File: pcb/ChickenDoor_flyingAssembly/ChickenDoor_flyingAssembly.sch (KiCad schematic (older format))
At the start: 3 parts

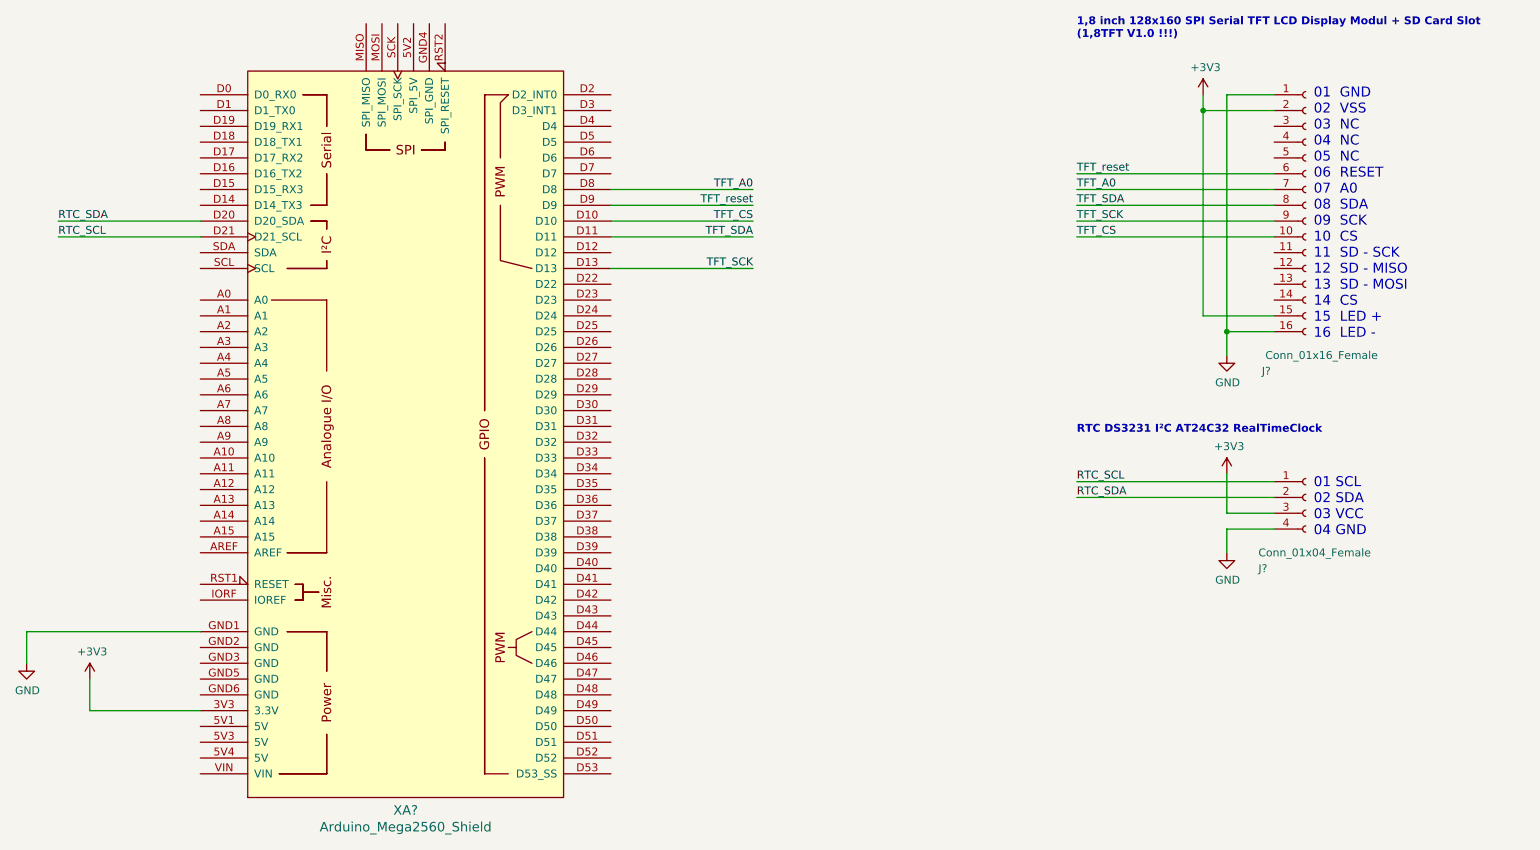
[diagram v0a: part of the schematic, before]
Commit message: some small changes in the schematic of the flying assembly.
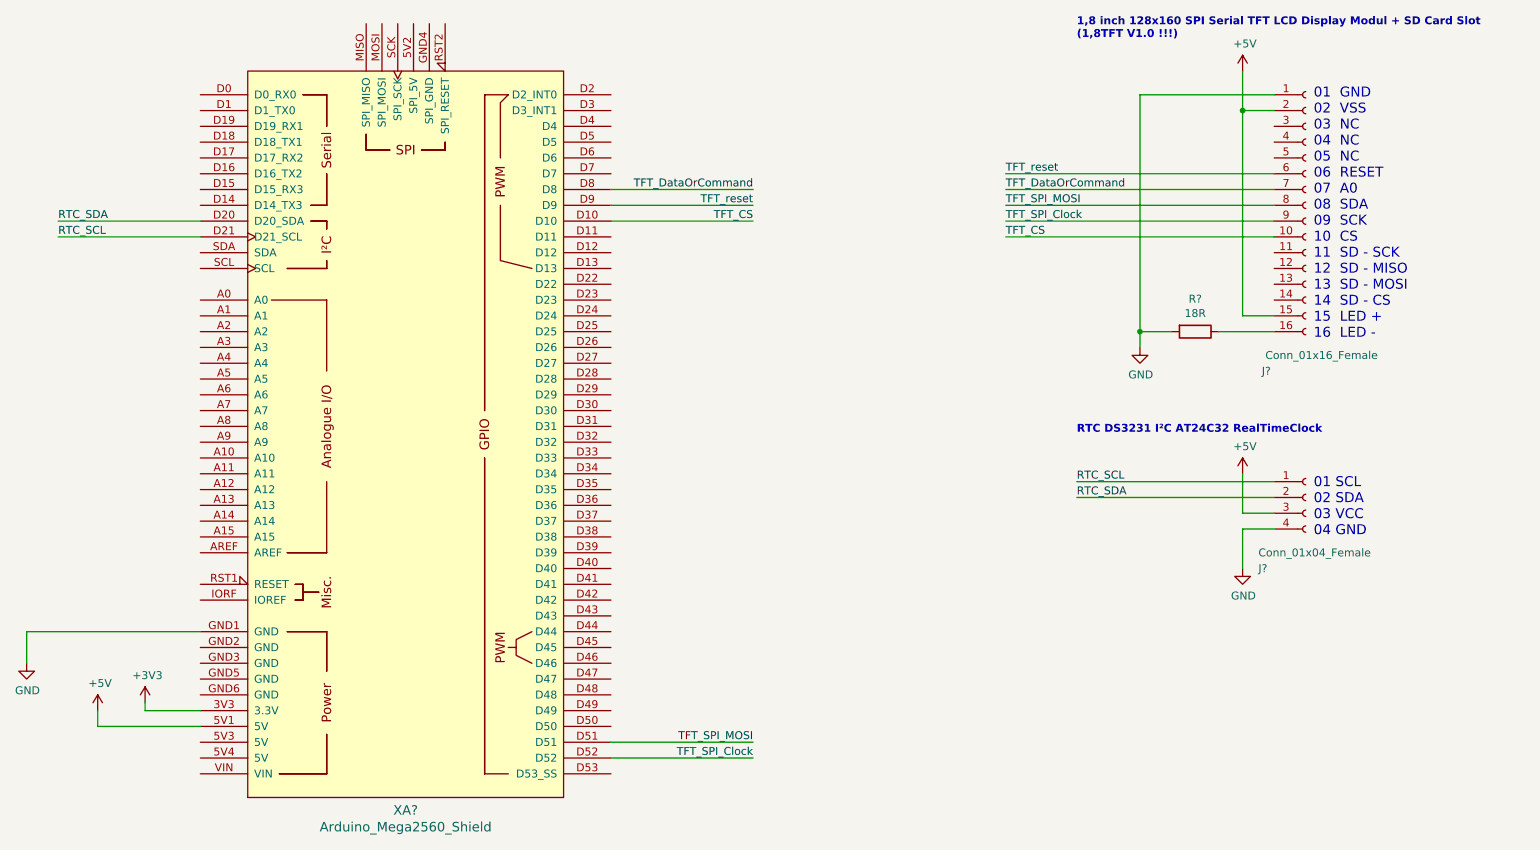
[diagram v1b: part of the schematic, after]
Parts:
- added R?: 18R, symbol Device:R
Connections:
- net +3V3: no longer J?.15 (Pin_15), J?.2 (Pin_2), J?.3 (Pin_3)
- net GND: now also R?.2; no longer J?.16 (Pin_16)
- net +5V: now reaches XA?.5V1 (5V)
- net +5V: now also J?.15 (Pin_15), J?.2 (Pin_2), J?.3 (Pin_3)
- net TFT_SPI_MOSI: now reaches XA?.D51
- net TFT_SPI_MOSI: now also J?.8 (Pin_8)
- net TFT_SPI_Clock: now reaches XA?.D52
- net TFT_SPI_Clock: now also J?.9 (Pin_9)
- net TFT_A0 renamed TFT_DataOrCommand
- net TFT_SCK: no longer names the net of XA?.D13
- net TFT_SCK: no longer J?.9 (Pin_9)
- net TFT_SDA: no longer names the net of XA?.D11
- net TFT_SDA: no longer J?.8 (Pin_8)
- new net: J?.16 (Pin_16), R?.1
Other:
- note added: "01 GND\n02 VSS\n03 NC\n04 NC\n05 NC\n06 RESET\n07 A0\n08 SDA\n09 SCK\n10 CS\n11 SD - SCK\n12 SD - MISO\n13 SD - MOSI\n14 SD - CS\n15 LED +\n16 LED -"
- note removed: "01 GND\n02 VSS\n03 NC\n04 NC\n05 NC\n06 RESET\n07 A0\n08 SDA\n09 SCK\n10 CS\n11 SD - SCK\n12 SD - MISO\n13 SD - MOSI\n14 CS\n15 LED +\n16 LED -"
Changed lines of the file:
@@
 L power:GND #PWR?
 U 1 1 5EDDCCDC
-P 8900 3250
-F 0 "#PWR?" H 8900 3000 50  0001 C CNN
-F 1 "GND" H 8905 3077 50  0000 C CNN
-F 2 "" H 8900 3250 50  0001 C CNN
-F 3 "" H 8900 3250 50  0001 C CNN
-	1    8900 3250
+P 8350 3200
+F 0 "#PWR?" H 8350 2950 50  0001 C CNN
+F 1 "GND" H 8355 3027 50  0000 C CNN
+F 2 "" H 8350 3200 50  0001 C CNN
+F 3 "" H 8350 3200 50  0001 C CNN
+	1    8350 3200
 	1    0    0    -1
 $EndComp
 Wire Wire Line
-	8900 3250 8900 3100
+	8350 3200 8350 3100
 Wire Wire Line
-	8900 3100 9200 3100
+	8350 3100 8550 3100
 Wire Wire Line
-	8900 3100 8900 1600
+	8350 3100 8350 1600
 Wire Wire Line
-	8900 1600 9200 1600
+	8350 1600 9200 1600
 $Comp
 L power:+3V3 #PWR?
 U 1 1 5EDDDAF5
-P 1700 5300
-F 0 "#PWR?" H 1700 5150 50  0001 C CNN
-F 1 "+3V3" H 1715 5473 50  0000 C CNN
-F 2 "" H 1700 5300 50  0001 C CNN
-F 3 "" H 1700 5300 50  0001 C CNN
-	1    1700 5300
+P 2050 5450
+F 0 "#PWR?" H 2050 5300 50  0001 C CNN
+F 1 "+3V3" H 2065 5623 50  0000 C CNN
+F 2 "" H 2050 5450 50  0001 C CNN
+F 3 "" H 2050 5450 50  0001 C CNN
+	1    2050 5450
 	1    0    0    -1
 $EndComp
 Wire Wire Line
-	2400 5500 1700 5500
+	2400 5500 2050 5500
 Wire Wire Line
-	1700 5500 1700 5300
-Connection ~ 8900 3100
-$Comp
-L power:+3V3 #PWR?
-U 1 1 5EDDF72B
-P 8750 1600
-F 0 "#PWR?" H 8750 1450 50  0001 C CNN
-F 1 "+3V3" H 8765 1773 50  0000 C CNN
-F 2 "" H 8750 1600 50  0001 C CNN
-F 3 "" H 8750 1600 50  0001 C CNN
-	1    8750 1600
-	1    0    0    -1
-$EndComp
+	2050 5500 2050 5450
+Connection ~ 8350 3100
+Text Notes 9450 3150 0    63   ~ 0
+01  GND\n02  VSS\n03  NC\n04  NC\n05  NC\n06  RESET\n07  A0\n08  SDA\n09  SCK\n10  CS\n11  SD - SCK\n12  SD - MISO\n13  SD - MOSI\n14  SD - CS\n15  LED +\n16  LED -
 Wire Wire Line
-	9200 1700 8750 1700
+	9200 3000 9000 3000
 Wire Wire Line
-	8750 1700 8750 1600
-Text Notes 9450 3150 0    63   ~ 0
-01  GND\n02  VSS\n03  NC\n04  NC\n05  NC\n06  RESET\n07  A0\n08  SDA\n09  SCK\n10  CS\n11  SD - SCK\n12  SD - MISO\n13  SD - MOSI\n14  CS\n15  LED +\n16  LED -
+	9200 2100 7500 2100
 Wire Wire Line
-	9200 3000 8750 3000
+	9200 2200 7500 2200
 Wire Wire Line
-	8750 3000 8750 1700
-Connection ~ 8750 1700
+	9200 2300 7500 2300
 Wire Wire Line
-	9200 2100 7950 2100
+	9200 2400 7500 2400
 Wire Wire Line
-	9200 2200 7950 2200
-Wire Wire Line
-	9200 2300 7950 2300
-Wire Wire Line
-	9200 2400 7950 2400
-Wire Wire Line
-	9200 2500 7950 2500
-Text Label 7950 2100 0    50   ~ 0
+	9200 2500 7500 2500
+Text Label 7500 2100 0    50   ~ 0
 TFT_reset
-Text Label 7950 2200 0    50   ~ 0
-TFT_A0
-Text Label 7950 2300 0    50   ~ 0
-TFT_SDA
-Text Label 7950 2400 0    50   ~ 0
-TFT_SCK
-Text Label 7950 2500 0    50   ~ 0
+Text Label 7500 2200 0    50   ~ 0
+TFT_DataOrCommand
+Text Label 7500 2300 0    50   ~ 0
+TFT_SPI_MOSI
+Text Label 7500 2400 0    50   ~ 0
+TFT_SPI_Clock
+Text Label 7500 2500 0    50   ~ 0
 TFT_CS
 Wire Wire Line
@@
 	5000 2400 5900 2400
 Wire Wire Line
-	5000 2500 5900 2500
+	5000 5700 5900 5700
 Wire Wire Line
-	5000 2700 5900 2700
+	5000 5800 5900 5800
 Text Label 5900 2200 2    50   ~ 0
-TFT_A0
+TFT_DataOrCommand
 Text Label 5900 2300 2    50   ~ 0
 TFT_reset
 Text Label 5900 2400 2    50   ~ 0
 TFT_CS
-Text Label 5900 2500 2    50   ~ 0
-TFT_SDA
-Text Label 5900 2700 2    50   ~ 0
-TFT_SCK
+Text Label 5900 5700 2    50   ~ 0
+TFT_SPI_MOSI
+Text Label 5900 5800 2    50   ~ 0
+TFT_SPI_Clock
 Text Notes 7950 1250 0    50   ~ 10
 1,8 inch 128x160 SPI Serial TFT LCD Display Modul + SD Card Slot\n(1,8TFT V1.0 !!!)
@@
 L power:GND #PWR?
 U 1 1 5EE1931E
-P 8900 4500
-F 0 "#PWR?" H 8900 4250 50  0001 C CNN
-F 1 "GND" H 8905 4327 50  0000 C CNN
-F 2 "" H 8900 4500 50  0001 C CNN
-F 3 "" H 8900 4500 50  0001 C CNN
-	1    8900 4500
+P 9000 4600
+F 0 "#PWR?" H 9000 4350 50  0001 C CNN
+F 1 "GND" H 9005 4427 50  0000 C CNN
+F 2 "" H 9000 4600 50  0001 C CNN
+F 3 "" H 9000 4600 50  0001 C CNN
+	1    9000 4600
 	1    0    0    -1
 $EndComp
 Wire Wire Line
-	9200 4350 8900 4350
+	9200 4350 9000 4350
 Wire Wire Line
-	8900 4350 8900 4500
-$Comp
-L power:+3V3 #PWR?
-U 1 1 5EE1A261
-P 8900 4000
-F 0 "#PWR?" H 8900 3850 50  0001 C CNN
-F 1 "+3V3" H 8915 4173 50  0000 C CNN
-F 2 "" H 8900 4000 50  0001 C CNN
-F 3 "" H 8900 4000 50  0001 C CNN
-	1    8900 4000
-	1    0    0    -1
-$EndComp
+	9000 4350 9000 4600
 Wire Wire Line
-	9200 4250 8900 4250
+	9200 4250 9000 4250
 Wire Wire Line
-	8900 4250 8900 4000
+	9000 4250 9000 4000
 Wire Wire Line
 	9200 4050 7950 4050
@@
 Wire Wire Line
 	2400 2400 1500 2400
+Wire Wire Line
+	9000 1450 9000 1700
+$Comp
+L Device:R R?
+U 1 1 5EE28B8A
+P 8700 3100
+F 0 "R?" V 8493 3100 50  0000 C CNN
+F 1 "18R" V 8584 3100 50  0000 C CNN
+F 2 "" V 8630 3100 50  0001 C CNN
+F 3 "~" H 8700 3100 50  0001 C CNN
+	1    8700 3100
+	0    1    1    0
+$EndComp
+Wire Wire Line
+	8850 3100 9200 3100
+$Comp
+L power:+5V #PWR?
+U 1 1 5EE38FDB
+P 1750 5500
+F 0 "#PWR?" H 1750 5350 50  0001 C CNN
+F 1 "+5V" H 1765 5673 50  0000 C CNN
+F 2 "" H 1750 5500 50  0001 C CNN
+F 3 "" H 1750 5500 50  0001 C CNN
+	1    1750 5500
+	1    0    0    -1
+$EndComp
+Wire Wire Line
+	2400 5600 1750 5600
+Wire Wire Line
+	1750 5600 1750 5500
+$Comp
+L power:+5V #PWR?
+U 1 1 5EE3C499
+P 9000 1450
+F 0 "#PWR?" H 9000 1300 50  0001 C CNN
+F 1 "+5V" H 9015 1623 50  0000 C CNN
+F 2 "" H 9000 1450 50  0001 C CNN
+F 3 "" H 9000 1450 50  0001 C CNN
+	1    9000 1450
+	1    0    0    -1
+$EndComp
+Wire Wire Line
+	9200 1700 9000 1700
+Connection ~ 9000 1700
+Wire Wire Line
+	9000 1700 9000 3000
+$Comp
+L power:+5V #PWR?
+U 1 1 5EE41E7D
+P 9000 4000
+F 0 "#PWR?" H 9000 3850 50  0001 C CNN
+F 1 "+5V" H 9015 4173 50  0000 C CNN
+F 2 "" H 9000 4000 50  0001 C CNN
+F 3 "" H 9000 4000 50  0001 C CNN
+	1    9000 4000
+	1    0    0    -1
+$EndComp
 $EndSCHEMATC

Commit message: Finished the DoorWidget with some (for this poor environment) fancy animations.
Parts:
- added R?: 10k, symbol Device:R
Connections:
- net +5V: now also R?.1
- net TFT_reset: now also R?.2
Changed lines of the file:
@@
 	9200 3000 9000 3000
 Wire Wire Line
-	9200 2100 7500 2100
+	9200 2100 8050 2100
 Wire Wire Line
-	9200 2200 7500 2200
+	9200 2200 7250 2200
 Wire Wire Line
-	9200 2300 7500 2300
+	9200 2300 7250 2300
 Wire Wire Line
-	9200 2400 7500 2400
+	9200 2400 7250 2400
 Wire Wire Line
-	9200 2500 7500 2500
-Text Label 7500 2100 0    50   ~ 0
+	9200 2500 7250 2500
+Text Label 7250 2100 0    50   ~ 0
 TFT_reset
-Text Label 7500 2200 0    50   ~ 0
+Text Label 7250 2200 0    50   ~ 0
 TFT_DataOrCommand
-Text Label 7500 2300 0    50   ~ 0
+Text Label 7250 2300 0    50   ~ 0
 TFT_SPI_MOSI
-Text Label 7500 2400 0    50   ~ 0
+Text Label 7250 2400 0    50   ~ 0
 TFT_SPI_Clock
-Text Label 7500 2500 0    50   ~ 0
+Text Label 7250 2500 0    50   ~ 0
 TFT_CS
 Wire Wire Line
@@
 	2400 2400 1500 2400
 Wire Wire Line
-	9000 1450 9000 1700
+	9000 1450 9000 1500
 $Comp
 L Device:R R?
@@
 	1    0    0    -1
 $EndComp
+$Comp
+L Device:R R?
+U 1 1 5EE6340C
+P 8050 1750
+F 0 "R?" H 8120 1796 50  0000 L CNN
+F 1 "10k" H 8120 1705 50  0000 L CNN
+F 2 "" V 7980 1750 50  0001 C CNN
+F 3 "~" H 8050 1750 50  0001 C CNN
+	1    8050 1750
+	1    0    0    -1
+$EndComp
+Wire Wire Line
+	9000 1500 8050 1500
+Wire Wire Line
+	8050 1500 8050 1600
+Connection ~ 9000 1500
+Wire Wire Line
+	9000 1500 9000 1700
+Wire Wire Line
+	8050 1900 8050 2100
+Connection ~ 8050 2100
+Wire Wire Line
+	8050 2100 7250 2100
 $EndSCHEMATC

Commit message: Added button functionality for next steps. Some cleanups in the project lib dependencies.
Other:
- note added: "D22 - D25 sind jetzt mal Taster drauf"
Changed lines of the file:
@@
 Wire Wire Line
 	8050 2100 7250 2100
+Text Notes 5300 3000 0    50   ~ 0
+D22 - D25 sind jetzt mal Taster drauf
 $EndSCHEMATC

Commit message: Added key event listener
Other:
- note added: "D22 - back \nD24 - enter\nD26 - up\nD28 - down"
- note removed: "D22 - D25 sind jetzt mal Taster drauf"
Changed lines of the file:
@@
 	8050 2100 7250 2100
 Text Notes 5300 3000 0    50   ~ 0
-D22 - D25 sind jetzt mal Taster drauf
+D22 - back \nD24 - enter\nD26 - up\nD28 - down
 $EndSCHEMATC
